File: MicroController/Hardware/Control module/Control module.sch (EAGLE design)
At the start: 97 parts, among them J2 0446200002, J3 0446200002, J4 0446200002, Q1 BSS138, Q10 BSS138, Q11 BSS138, Q12 BSS138, Q2 BSS138, Q3 BSS138, Q4 BSS138, Q5 BSS138, Q6 BSS138, Q7 BSS138, Q8 BSS138, Q9 BSS138, T1 SI4804CDY-T1-GE3, U1 XMEGA-A3-AU, U3 TLV1117-33CDCY, U4 CD4051BM, U6 TXB0108PWR, U7 TXB0108PWR, U8 LM2937IMP-5.0, U9 CD74HC4067SM96

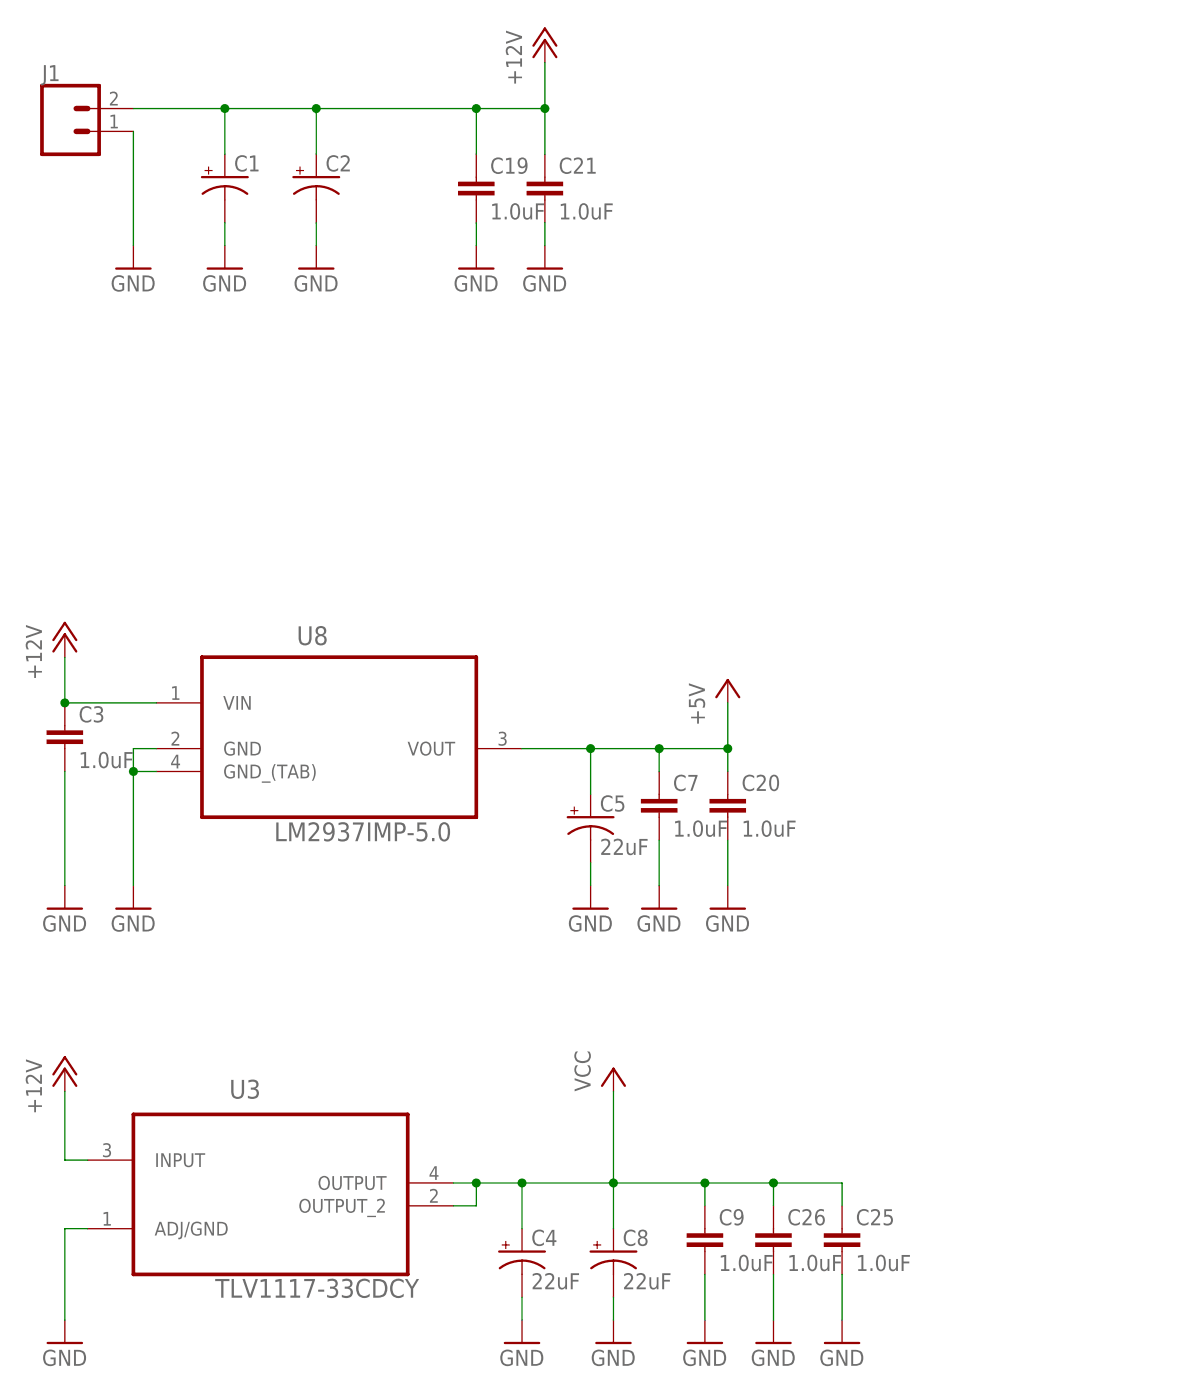
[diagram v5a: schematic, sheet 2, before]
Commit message: Finished the Control PCB version 2.0
Not a lot of changes where made comparing to the previous version of the PCB. Most noticeably the way the fans are controlled has changed. Further some small things that where found out during tests with the previous version.
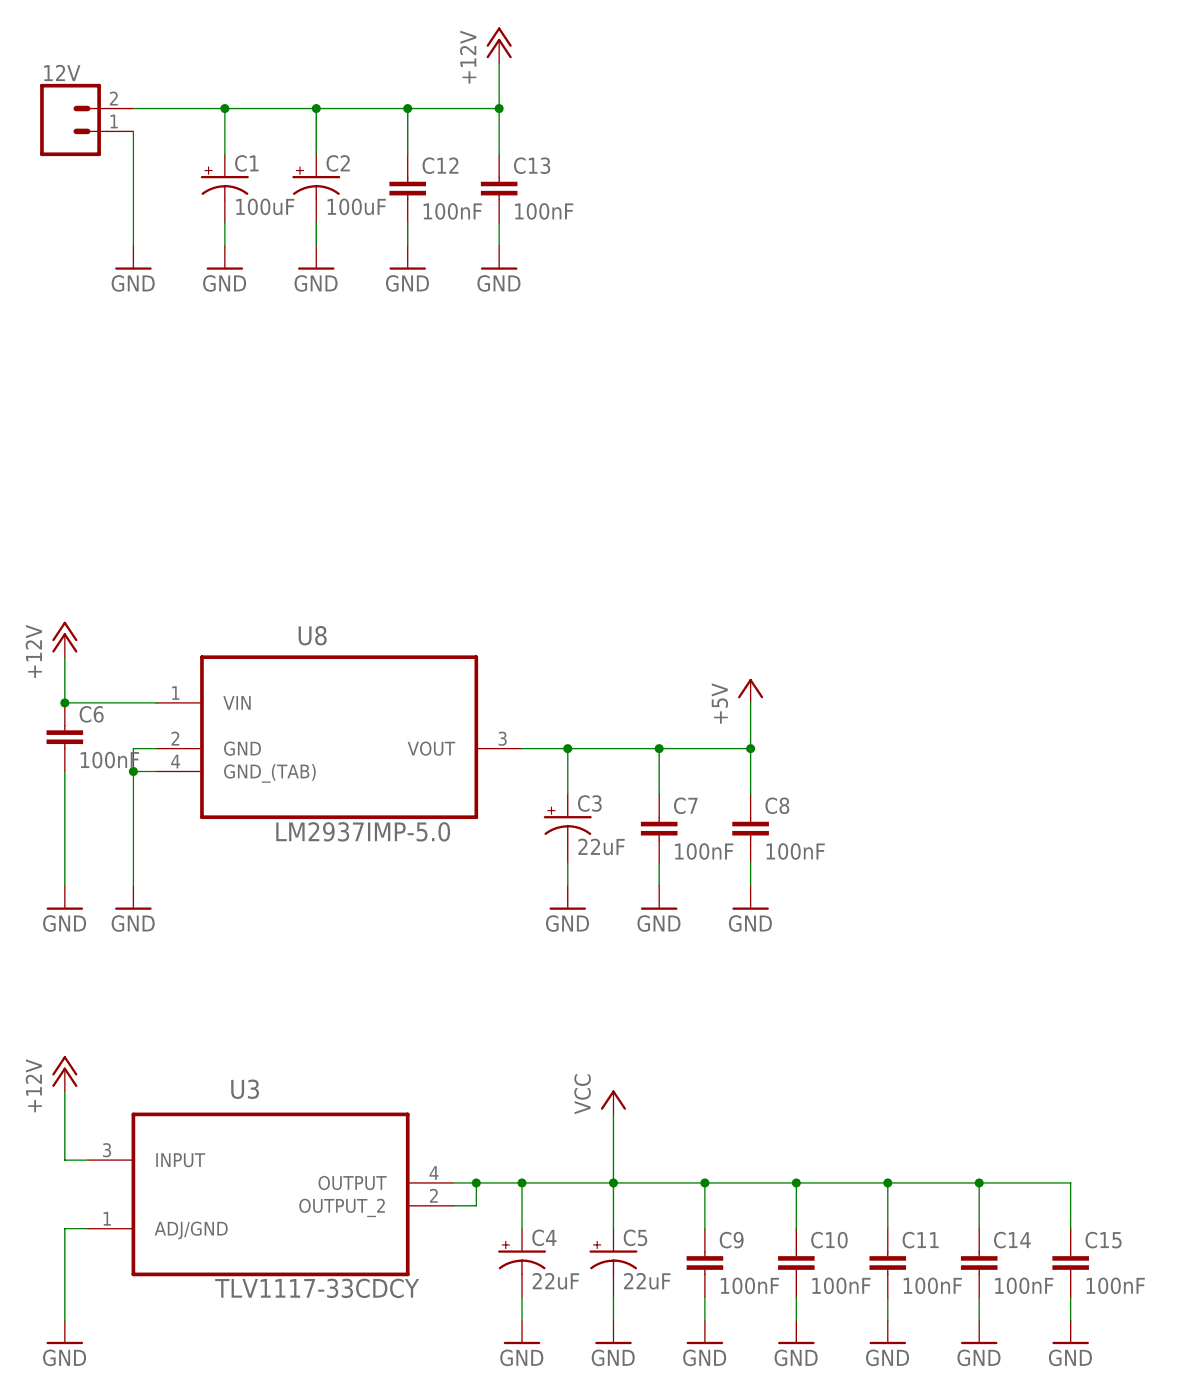
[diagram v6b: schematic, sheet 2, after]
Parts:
- removed C19, C20, C21, C25, C26: 1.0uF, SparkFun-Capacitors:1.0UF-0805-25V-(+80/-20%)
- added C10, C11, C12, C13, C14, C15, C6: 100nF, SparkFun-Capacitors:1.0UF-0805-25V-(+80/-20%)
- C1, C2: value (none) -> 100uF
- C3: value 1.0uF -> 22uF; device SparkFun-Capacitors:1.0UF-0805-25V-(+80/-20%) -> adafruit:CPOL-US153CLV-0505
- C7, C9: value 1.0uF -> 100nF
- C8: value 22uF -> 100nF; device adafruit:CPOL-US153CLV-0505 -> SparkFun-Capacitors:1.0UF-0805-25V-(+80/-20%)
- renumbered COMMUNICATION to RJ45_COMM, J1 to 12V, J2 to RJ45_WHITE, J3 to RJ45_BLUE, J4 to RJ45_RED
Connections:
- net +12V: now also C12.1, C13.1, C6.1; no longer C19.1, C21.1, C3.1
- net +5V: now also C3.+, C8.1; no longer C20.1, C5.+
- net GND: now also C10.2, C11.2, C12.2, C13.2, C14.2, C15.2, C3.-, C6.2, C8.2; no longer C19.2, C20.2, C21.2, C25.2, C26.2, C3.2, C8.-
- net VCC: now also C10.1, C11.1, C14.1, C15.1, C5.+; no longer C25.1, C26.1, C8.+
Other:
- moved on the sheet: C5, C7, C9
